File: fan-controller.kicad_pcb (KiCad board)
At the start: 2 copper layers, 33 x 16 mm, 17 parts, among them J1 PWR, J2 PTC, J3 FAN, J4 Prog, Q1 AO3401A, U1 PY32F002A

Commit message: Fix ERC
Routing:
- net +3.3V: track 24.8 -> 23.4 mm
- net VPP: track 26.6 -> 25.4 mm
- net Net-(C3-Pad1): track 12.1 -> 11.0 mm
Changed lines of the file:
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@@
     (tags "inductor abracon smd shielded")
     (property "LCSC" "C38117")
-    (property "Sheetfile" "/home/user/dev/hardware/fan-controller/fan-controller.sch")
+    (property "Sheetfile" "fan-controller.kicad_sch")
     (property "Sheetname" "")
     (attr smd)
@@
     (tags "resistor")
     (property "LCSC" "C25803")
-    (property "Sheetfile" "/home/user/dev/hardware/fan-controller/fan-controller.sch")
+    (property "Sheetfile" "fan-controller.kicad_sch")
     (property "Sheetname" "")
     (attr smd)
@@
     (property "Description" "50V+")
     (property "LCSC" "C13585")
-    (property "Sheetfile" "/home/user/dev/hardware/fan-controller/fan-controller.sch")
+    (property "Sheetfile" "fan-controller.kicad_sch")
     (property "Sheetname" "")
     (attr smd)
@@
   )
   (footprint "Resistor_SMD:R_1206_3216Metric" (layer "F.Cu")
-    (at 122 63 180)
+    (at 122.05 63 180)
     (descr "Resistor SMD 1206 (3216 Metric), square (rectangular) end terminal, IPC_7351 nominal, (Body size source: IPC-SM-782 page 72, https://www.pcb-3d.com/wordpress/wp-content/uploads/ipc-sm-782a_amendment_1_and_2.pdf), generated with kicad-footprint-generator")
     (tags "resistor")
     (property "Description" "50V+")
     (property "LCSC" "C13585")
-    (property "Sheetfile" "/home/user/dev/hardware/fan-controller/fan-controller.sch")
+    (property "Sheetfile" "fan-controller.kicad_sch")
     (property "Sheetname" "")
     (attr smd)
@@
     (descr "Through hole straight pin header, 1x02, 2.54mm pitch, single row")
     (tags "Through hole pin header THT 1x02 2.54mm single row")
-    (property "Sheetfile" "/home/user/dev/hardware/fan-controller/fan-controller.sch")
+    (property "Sheetfile" "fan-controller.kicad_sch")
     (property "Sheetname" "")
     (attr through_hole)
@@
     (descr "Through hole straight pin header, 1x02, 2.54mm pitch, single row")
     (tags "Through hole pin header THT 1x02 2.54mm single row")
-    (property "Sheetfile" "/home/user/dev/hardware/fan-controller/fan-controller.sch")
+    (property "Sheetfile" "fan-controller.kicad_sch")
     (property "Sheetname" "")
     (attr through_hole)
@@
     (tags "Diode Mini-MELF (SOD-80)")
     (property "LCSC" "C8056")
-    (property "Sheetfile" "/home/user/dev/hardware/fan-controller/fan-controller.sch")
+    (property "Sheetfile" "fan-controller.kicad_sch")
     (property "Sheetname" "")
     (attr smd)
@@
     (descr "Through hole straight pin header, 1x04, 2.54mm pitch, single row")
     (tags "Through hole pin header THT 1x04 2.54mm single row")
-    (property "Sheetfile" "/home/user/dev/hardware/fan-controller/fan-controller.sch")
+    (property "Sheetfile" "fan-controller.kicad_sch")
     (property "Sheetname" "")
     (attr through_hole)
@@
     (attr board_only exclude_from_pos_files exclude_from_bom)
     (fp_text reference "kibuzzard-63E17401" (at 0 -4.233917 90) (layer "F.SilkS") hide
-      (effects (font (size 0 0)))
+      (effects (font (size 0 0) (thickness 0.15)))
     )
     (fp_text value "G***" (at 0 4.233917 90) (layer "F.SilkS") hide
-      (effects (font (size 0 0)))
+      (effects (font (size 0 0) (thickness 0.15)))
     )
     (fp_poly (pts
@@
     (tags "resistor")
     (property "LCSC" "C25804")
-    (property "Sheetfile" "/home/user/dev/hardware/fan-controller/fan-controller.sch")
+    (property "Sheetfile" "fan-controller.kicad_sch")
     (property "Sheetname" "")
     (attr smd)
@@
     (attr board_only exclude_from_pos_files exclude_from_bom)
     (fp_text reference "kibuzzard-63E173EF" (at 0 -4.184695 90) (layer "F.SilkS") hide
-      (effects (font (size 0 0)))
+      (effects (font (size 0 0) (thickness 0.15)))
     )
     (fp_text value "G***" (at 0 4.184695 90) (layer "F.SilkS") hide
-      (effects (font (size 0 0)))
+      (effects (font (size 0 0) (thickness 0.15)))
     )
     (fp_poly (pts
@@
     (property "Description" "50V+")
     (property "LCSC" "C13585")
-    (property "Sheetfile" "/home/user/dev/hardware/fan-controller/fan-controller.sch")
+    (property "Sheetfile" "fan-controller.kicad_sch")
     (property "Sheetname" "")
     (attr smd)
@@
     (tags "Diode SMA (DO-214AC)")
     (property "LCSC" "C2480")
-    (property "Sheetfile" "/home/user/dev/hardware/fan-controller/fan-controller.sch")
+    (property "Sheetfile" "fan-controller.kicad_sch")
     (property "Sheetname" "")
     (attr smd)
@@
     (attr board_only exclude_from_pos_files exclude_from_bom)
     (fp_text reference "kibuzzard-63E173E4" (at 0 -4.184695 90) (layer "F.SilkS") hide
-      (effects (font (size 0 0)))
+      (effects (font (size 0 0) (thickness 0.15)))
     )
     (fp_text value "G***" (at 0 4.184695 90) (layer "F.SilkS") hide
-      (effects (font (size 0 0)))
+      (effects (font (size 0 0) (thickness 0.15)))
     )
     (fp_poly (pts
@@
     (tags "SOIC SO")
     (property "LCSC" "C5128435")
-    (property "Sheetfile" "/home/user/dev/hardware/fan-controller/fan-controller.sch")
+    (property "Sheetfile" "fan-controller.kicad_sch")
     (property "Sheetname" "")
     (attr smd)
@@
       (net 1 "+3.3V") (pinfunction "VCC") (pintype "power_in"))
     (pad "2" smd roundrect (at -2.475 -0.635) (size 1.95 0.6) (layers "F.Cu" "F.Paste" "F.Mask") (roundrect_rratio 0.25)
-      (net 10 "unconnected-(U1-Pad2)") (pinfunction "PA4/PA10") (pintype "bidirectional"))
+      (net 10 "unconnected-(U1-Pad2)") (pinfunction "PA4/PA10") (pintype "bidirectional+no_connect"))
     (pad "3" smd roundrect (at -2.475 0.635) (size 1.95 0.6) (layers "F.Cu" "F.Paste" "F.Mask") (roundrect_rratio 0.25)
       (net 5 "/TEMP_SENSE") (pinfunction "PA3") (pintype "bidirectional"))
@@
     (tags "SOT TO_SOT_SMD")
     (property "LCSC" "C15127")
-    (property "Sheetfile" "/home/user/dev/hardware/fan-controller/fan-controller.sch")
+    (property "Sheetfile" "fan-controller.kicad_sch")
     (property "Sheetname" "")
     (attr smd)
@@
     (descr "Through hole straight pin header, 1x02, 2.54mm pitch, single row")
     (tags "Through hole pin header THT 1x02 2.54mm single row")
-    (property "Sheetfile" "/home/user/dev/hardware/fan-controller/fan-controller.sch")
+    (property "Sheetfile" "fan-controller.kicad_sch")
     (property "Sheetname" "")
     (attr through_hole)
@@
   (segment (start 111.8 65) (end 112.9753 65) (width 0.25) (layer "F.Cu") (net 1))
   (segment (start 109.25 57.1753) (end 108.525 57.9003) (width 0.25) (layer "F.Cu") (net 1))
-  (segment (start 109.25 54.075) (end 109.175 54) (width 0.25) (layer "F.Cu") (net 1))
   (segment (start 111.0375 56) (end 109.25 56) (width 0.25) (layer "F.Cu") (net 1))
   (segment (start 109.25 56) (end 109.25 57.1753) (width 0.25) (layer "F.Cu") (net 1))
   (segment (start 112.9753 65) (end 114.783 63.1923) (width 0.25) (layer "F.Cu") (net 1))
-  (segment (start 112.7097 60.635) (end 113.475 60.635) (width 0.25) (layer "F.Cu") (net 1))
   (segment (start 109.25 57.1753) (end 112.7097 60.635) (width 0.25) (layer "F.Cu") (net 1))
-  (segment (start 113.933 60.635) (end 113.475 60.635) (width 0.25) (layer "F.Cu") (net 1))
-  (segment (start 108.525 58) (end 108.525 58.095) (width 0.25) (layer "F.Cu") (net 1))
   (segment (start 108.525 57.9003) (end 108.525 58) (width 0.25) (layer "F.Cu") (net 1))
   (segment (start 114.783 63.1923) (end 114.783 61.485) (width 0.25) (layer "F.Cu") (net 1))
@@
   (segment (start 122 63) (end 121 63) (width 0.25) (layer "F.Cu") (net 2))
   (segment (start 113.9625 56) (end 113.9625 57.0375) (width 0.25) (layer "F.Cu") (net 2))
-  (segment (start 113.9625 56) (end 114 56.0375) (width 0.25) (layer "F.Cu") (net 2))
   (segment (start 115.405 58.095) (end 115.5 58) (width 0.25) (layer "F.Cu") (net 2))
   (segment (start 113.475 58.095) (end 111.595 58.095) (width 0.25) (layer "F.Cu") (net 2))
@@
   (segment (start 116.0625 60.95) (end 116.0625 60.4625) (width 0.25) (layer "F.Cu") (net 3))
   (segment (start 116.4246 57.9644) (end 116.4246 54.25) (width 0.25) (layer "F.Cu") (net 3))
-  (segment (start 116 63) (end 116.0625 62.9375) (width 0.25) (layer "F.Cu") (net 3))
-  (segment (start 127.5 55) (end 126.3247 55) (width 0.25) (layer "F.Cu") (net 3))
   (segment (start 116.0625 62.9375) (end 116.0625 60.95) (width 0.25) (layer "F.Cu") (net 3))
   (segment (start 123 57.7253) (end 122 56.7253) (width 0.25) (layer "F.Cu") (net 4))
-  (segment (start 127.5 62) (end 126.3247 62) (width 0.25) (layer "F.Cu") (net 4))
   (segment (start 123.4625 59.9625) (end 123 59.5) (width 0.25) (layer "F.Cu") (net 4))
   (segment (start 123 59.5) (end 123 57.7253) (width 0.25) (layer "F.Cu") (net 4))
@@
   (segment (start 123.4625 62) (end 126.3247 62) (width 0.25) (layer "F.Cu") (net 4))
   (segment (start 122 55.5) (end 122 56.7253) (width 0.25) (layer "F.Cu") (net 4))
-  (segment (start 106 60.3575) (end 106 60.175) (width 0.25) (layer "F.Cu") (net 5))
   (segment (start 106 60.175) (end 102.825 60.175) (width 0.25) (layer "F.Cu") (net 5))
   (segment (start 108.525 60.635) (end 107.135 60.635) (width 0.25) (layer "F.Cu") (net 5))
@@
   (segment (start 110.6229 61.905) (end 113.475 61.905) (width 0.25) (layer "F.Cu") (net 6))
   (segment (start 107.5279 65) (end 110.6229 61.905) (width 0.25) (layer "F.Cu") (net 6))
-  (segment (start 108.1209 61.905) (end 108.525 61.905) (width 0.25) (layer "F.Cu") (net 7))
   (segment (start 105.0259 65) (end 108.1209 61.905) (width 0.25) (layer "F.Cu") (net 7))
   (segment (start 104.18 65) (end 105.0259 65) (width 0.25) (layer "F.Cu") (net 7))

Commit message: Final touch-ups
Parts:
- removed C2: 10u, Resistor_SMD:R_1206_3216Metric
- removed D1: ZMM3V3-M, Diode_SMD:D_MiniMELF
- removed R1: 10k, Resistor_SMD:R_0603_1608Metric
- added C4: 10u, Resistor_SMD:R_1206_3216Metric, F.Cu at (113.1, 53.6)
- added U2: L78L05, Package_TO_SOT_SMD:SOT-89-3, F.Cu at (107.9, 54.8)
- J4: value Prog -> Conn_ARM_SWD_TagConnect_TC2030-NL; footprint Connector_PinHeader_2.54mm:PinHeader_1x04_P2.54mm_Vertical -> Connector:Tag-Connect_TC2030-IDC-NL_2x03_P1.27mm_Vertical
- moved J4 0.81 mm to (111.0, 64.9), turned to 0 degrees
- moved C1 0.60 mm to (113.1, 56.0)
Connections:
- J4 pad 2: GND -> /SWCLK
- J4 pad 3: /SWDIO -> unconnected-(J4-Pad3)
- J4 pad 4: /SWCLK -> /SWDIO
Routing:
- net GND: track 22.4 -> 17.4 mm
- net VPP: track 25.4 -> 30.4 mm
- net +3.3V: track 23.4 -> 28.1 mm
- net /SWCLK: track 5.22 -> 3.32 mm
- net Net-(C3-Pad1): track 11.0 -> 12.0 mm
- net /SWDIO: track 8.04 -> 7.53 mm

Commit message: Fix flyback diode & add output sense
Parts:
- added R1: 330k, Resistor_SMD:R_0603_1608Metric, F.Cu at (117.5, 64.0)
- added R3: 47k, Resistor_SMD:R_0603_1608Metric, F.Cu at (116.0, 64.0)
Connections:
- C3 pad 1: Net-(C3-Pad1) -> /FAN_OUT
- D2 pad 1: Net-(C3-Pad1) -> Net-(D2-K)
- J3 pad 1: Net-(C3-Pad1) -> /FAN_OUT
- L1 pad 1: Net-(L1-Pad1) -> Net-(D2-K)
- L1 pad 2: Net-(C3-Pad1) -> /FAN_OUT
- Q1 pad 3: Net-(L1-Pad1) -> Net-(D2-K)
- U1 pad 2: unconnected-(U1-Pad2) -> /FAN_SENSE
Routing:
- net /FAN_OUT: track 0.00 -> 15.2 mm
- net /FAN_SENSE: track 0.00 -> 13.9 mm, vias 0 -> 2
- net Net-(C3-Pad1): track 12.0 -> 0.00 mm
- net Net-(D2-K): track 0.00 -> 5.19 mm
- net Net-(L1-Pad1): track 1.86 -> 0.00 mm
- net GND: track 17.4 -> 18.6 mm, vias 12 -> 13

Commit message: hardware bug fixes
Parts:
- added R4: 47k, Resistor_SMD:R_0402_1005Metric, F.Cu at (106.0, 65.0)
- R1: renamed from R2; footprint Resistor_SMD:R_0603_1608Metric -> Resistor_SMD:R_0402_1005Metric
- R2: renamed from R3; footprint Resistor_SMD:R_0603_1608Metric -> Resistor_SMD:R_0402_1005Metric
- R3: renamed from R1; footprint Resistor_SMD:R_0603_1608Metric -> Resistor_SMD:R_0402_1005Metric
- renumbered C4 to C1, C1 to C2, D2 to D1, U2 to U1, U1 to U2, kibuzzard-63E173EF to kibuzzard-1, kibuzzard-63E17401 to kibuzzard-2, kibuzzard-63E173E4 to kibuzzard-3
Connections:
- J4 pad 2: /SWCLK -> /SWDIO
- J4 pad 3: unconnected-(J4-~{RESET}-Pad3) -> /~{RST}
- J4 pad 4: /SWDIO -> /SWCLK
- J4 pad 6: unconnected-(J4-SWO-Pad6) -> /~{RST}
- U2 pad 6: +3.3V -> /~{RST}
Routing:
- net /~{RST}: track 0.00 -> 14.1 mm, vias 0 -> 2
- net Net-(D1-K): track 5.19 -> 12.1 mm
- net /FAN_OUT: track 15.2 -> 19.0 mm
- net /FAN_SENSE: track 13.9 -> 11.2 mm, vias 2 -> 0
- net VPP: track 30.4 -> 32.9 mm
- net /SWDIO: track 7.53 -> 5.81 mm, vias 0 -> 2
- net +3.3V: track 28.1 -> 27.5 mm
- net /SWCLK: track 3.32 -> 3.89 mm

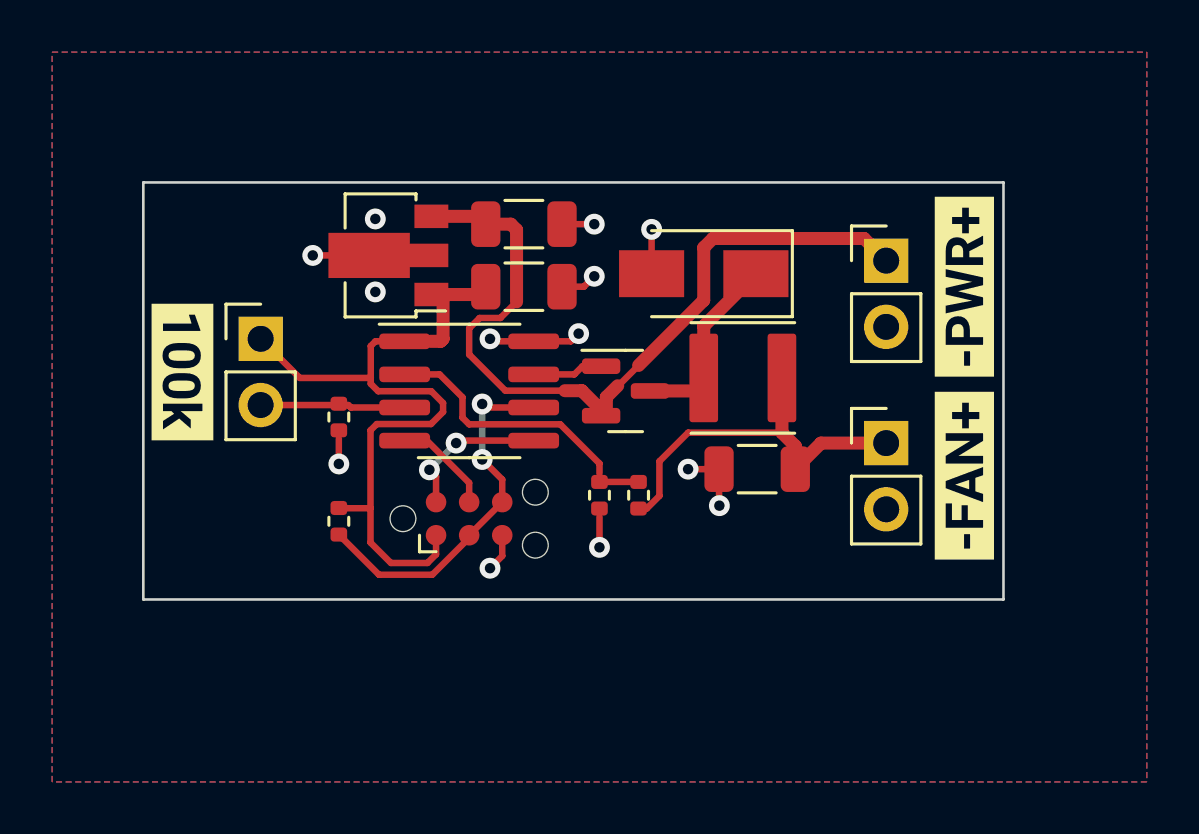
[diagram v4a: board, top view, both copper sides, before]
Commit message: Fix circuit mistakes
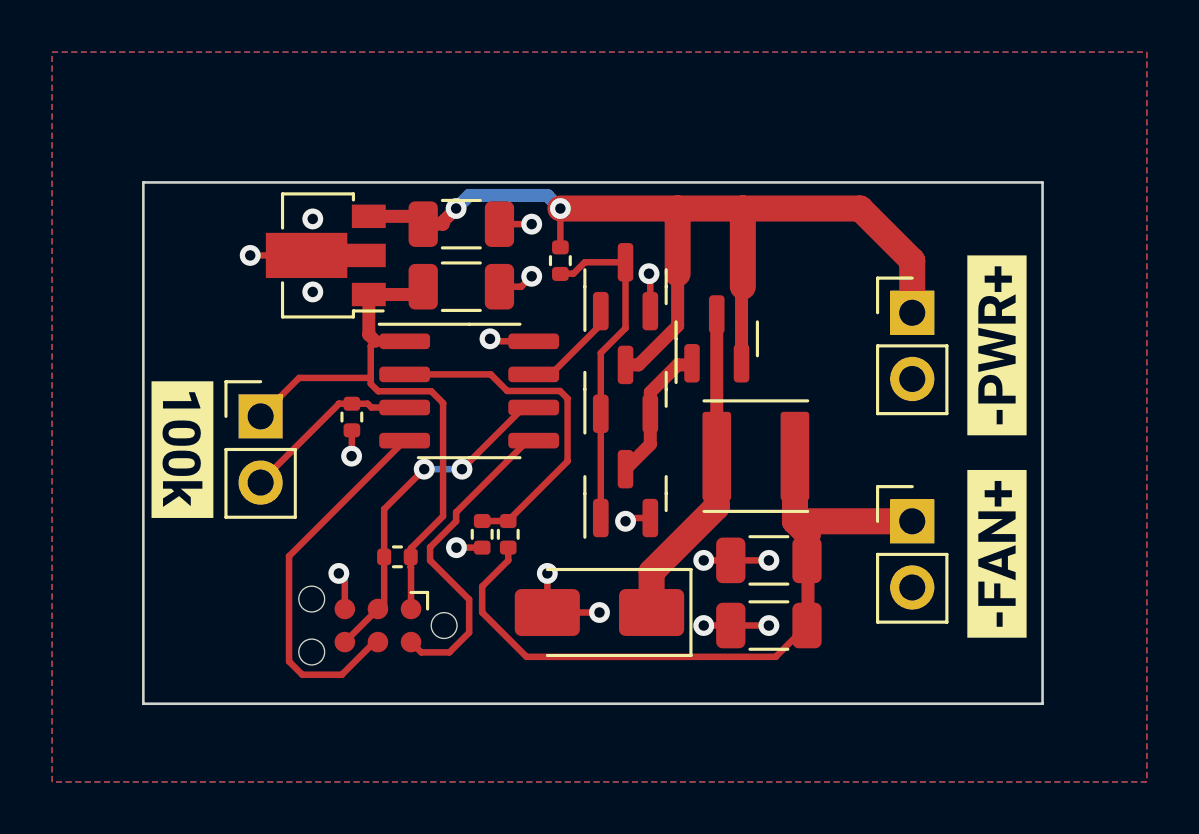
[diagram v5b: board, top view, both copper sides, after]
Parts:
- added C4: 10u, Resistor_SMD:R_1206_3216Metric, F.Cu at (122.5, 66.5)
- added Q2: MMBT5401, Package_TO_SOT_SMD:SOT-23, F.Cu at (117.0, 63.9)
- added Q3: MMBT5551, Package_TO_SOT_SMD:SOT-23, F.Cu at (117.0, 59.9)
- added Q4: MMBT5551, Package_TO_SOT_SMD:SOT-23, F.Cu at (117.0, 56.0)
- added R7: 22k, Resistor_SMD:R_0402_1005Metric, F.Cu at (114.5, 55.0)
- L1: value 10uH, 150mΩ -> 47u
- R2, R4: value 47k -> 22k
- R3: value 330k -> 100k
- moved D1 13.6 mm to (116.0, 68.5)
- moved C3 6.02 mm to (122.5, 69.0)
- moved J4 5.39 mm to (107.5, 69.0), turned to 180 degrees
- moved R3 5.22 mm to (112.5, 65.5)
- moved R2 4.74 mm to (111.5, 65.5)
- moved Q1 4.03 mm to (120.5, 58.0), turned to 90 degrees
- moved kibuzzard-3 3.25 mm to (131.2, 66.2)
- moved J3 3.16 mm to (128.0, 65.0)
- moved L1 3.04 mm to (122.0, 62.5)
- moved J2 2.98 mm to (103.0, 61.0)
- moved kibuzzard-2 2.98 mm to (100.0, 62.2)
- moved R4 2.63 mm to (108.2, 66.4), turned to 0 degrees
- moved kibuzzard-1 2.57 mm to (131.2, 58.2)
- moved U1 2.40 mm to (105.5, 54.8)
- moved C1 2.40 mm to (110.7, 53.6)
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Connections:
- Q1 pad 1: /SW -> Net-(Q1-G)
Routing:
- net Net-(Q2-B): track 0.00 -> 12.9 mm
- net /SWCLK: track 3.89 -> 14.5 mm
- net /FAN_OUT: track 19.0 -> 27.3 mm
- net VPP: track 32.9 -> 40.7 mm, vias 0 -> 2
- net /SWDIO: track 5.81 -> 12.2 mm, vias 2 -> 0
- net Net-(Q1-G): track 0.00 -> 5.33 mm
- net GND: track 18.6 -> 23.2 mm, vias 13 -> 17
- net +3.3V: track 27.5 -> 23.1 mm
- net /FAN_SENSE: track 11.2 -> 13.3 mm
- net /~{RST}: track 14.1 -> 12.5 mm
- net /TEMP_SENSE: track 5.56 -> 6.84 mm
- net /SW: track 2.72 -> 3.30 mm
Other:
- board size 33 x 16 mm -> 34.5 x 20 mm
- board text added: "flaviutamas.com/p/dc-fan-temp 5-24V Fan Temp Controller Ifan≤250mA"
- board text removed: "flaviutamas.com/p/dc-fan-temp 5-24V Fan Temp Controller Ifan≤500mA"
